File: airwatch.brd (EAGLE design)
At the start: 48.4 x 30.5 mm, 34 parts, among them IC1 MCP1825 (3.3 or 3v), IC2 TP4056, J1 POWER_JACK, Q1 NCV4274, U1 ESP8266-01/ESP-01, U2 ADS1015IDGSR

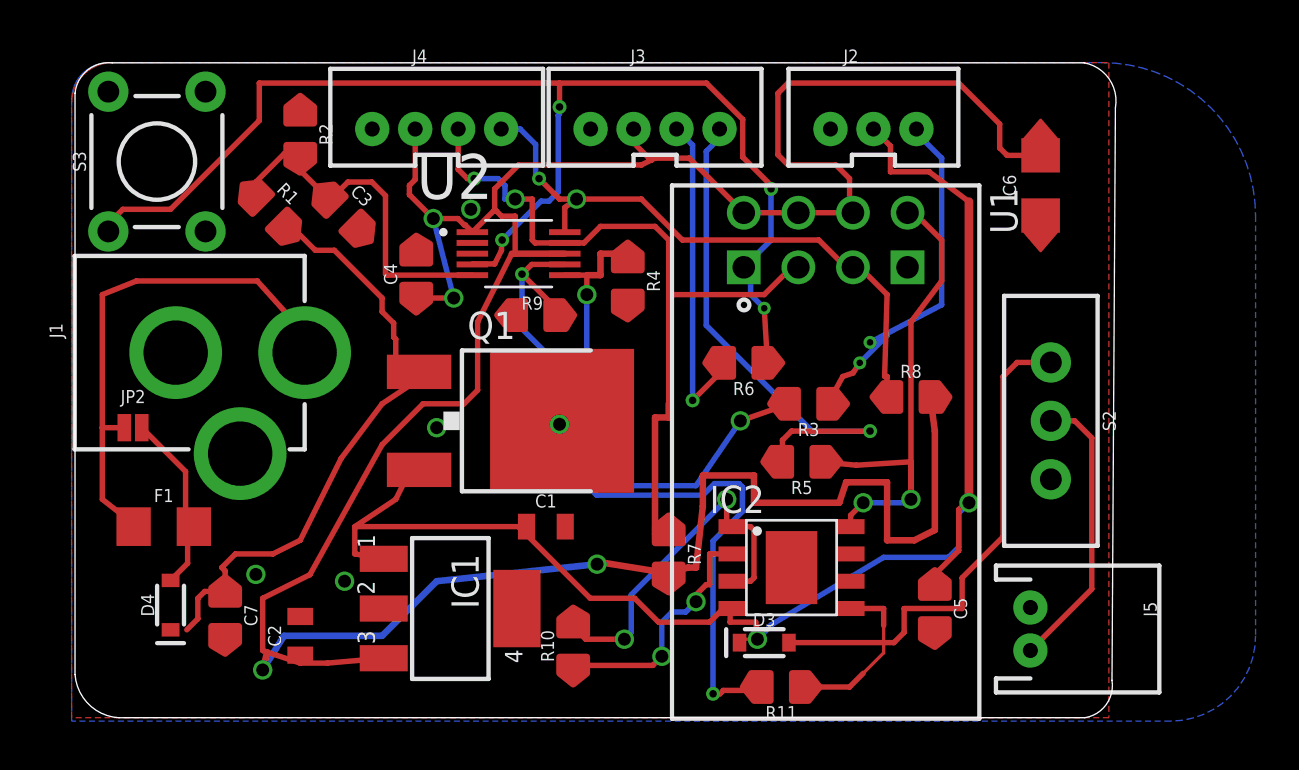
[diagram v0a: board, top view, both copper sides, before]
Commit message: Soldermask for the 0805-ez pads. Totally untested, might even revert.
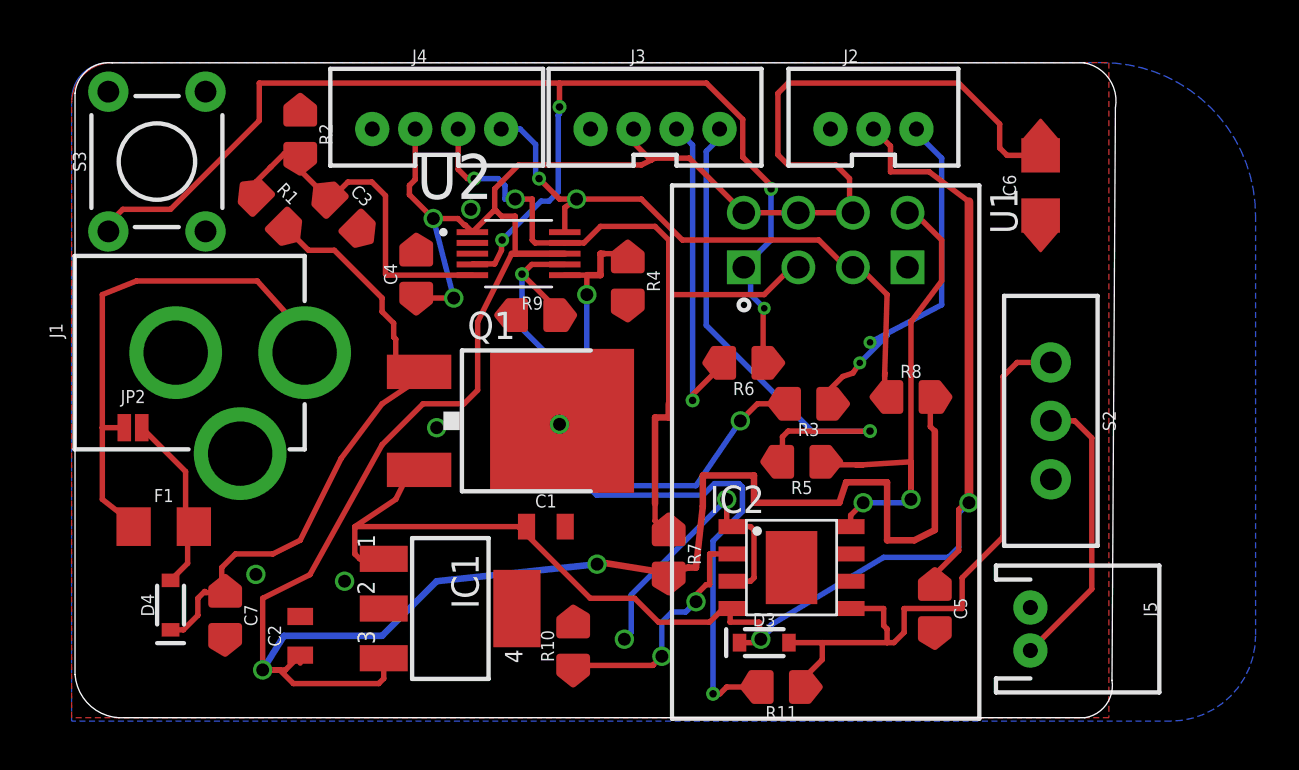
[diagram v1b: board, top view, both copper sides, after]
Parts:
- R5: value 220-2.2k -> (none)
- R6: value 470R-10k -> (none)
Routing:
- net VCC: track 142.3 -> 145.7 mm
- net GND: track 17.0 -> 14.4 mm
- net VBAT: track 31.6 -> 29.1 mm
